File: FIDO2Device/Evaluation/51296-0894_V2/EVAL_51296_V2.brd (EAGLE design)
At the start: 25 x 38 mm, 25 parts, among them CN1 51296-0894, CN2 IF_6PIN, CN3 IF_3PIN, CN4 IF_4PIN, Q1 BSS84AKQBZ, U1 RV-3028-C7

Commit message: レイアウトを修正
・裏面べたGNDのパターンを改善
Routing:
- net VDD: track 56.7 -> 61.6 mm, vias 5 -> 6
- net LED_R: track 36.8 -> 36.5 mm, vias 1 -> 2
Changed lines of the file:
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@@
 </element>
 <element name="R1" library="Parts" package="R0402N" value="5.1k" x="6.9" y="13.8" smashed="yes" rot="R180">
-<attribute name="NAME" x="8.3" y="13.5" size="0.6" layer="25"/>
+<attribute name="NAME" x="5.4" y="14" size="0.6" layer="25" rot="R180"/>
 <attribute name="VALUE" x="7.4" y="15.1" size="0.6" layer="27" rot="R180"/>
 </element>
 <element name="R2" library="Parts" package="R0402N" value="20k" x="6.9" y="12.2" smashed="yes">
-<attribute name="NAME" x="8.3" y="11.9" size="0.6" layer="25"/>
+<attribute name="NAME" x="5.4" y="12.4" size="0.6" layer="25" rot="R180"/>
 <attribute name="VALUE" x="6.4" y="10.9" size="0.6" layer="27"/>
 </element>
@@
 <via x="11.45" y="9" extent="1-16" drill="0.3"/>
 <via x="15.3" y="5.2" extent="1-16" drill="0.3"/>
-<via x="8.8" y="10" extent="1-16" drill="0.3"/>
-<wire x1="9" y1="9.8" x2="10.65" y2="9.8" width="0.2032" layer="16"/>
-<wire x1="11.45" y1="9" x2="10.65" y2="9.8" width="0.2032" layer="16"/>
+<via x="8.6" y="12.2" extent="1-16" drill="0.3"/>
 <wire x1="11.45" y1="7.8" x2="11.45" y2="9" width="0.2032" layer="1"/>
 <wire x1="15.3" y1="5.2" x2="13" y2="5.2" width="0.2032" layer="16"/>
@@
 <wire x1="13.55" y1="11.1" x2="11.45" y2="9" width="0.2032" layer="16"/>
 <wire x1="15.95" y1="10.95" x2="16.4" y2="11.4" width="0.2032" layer="1"/>
-<wire x1="9" y1="9.8" x2="8.8" y2="10" width="0.2032" layer="16"/>
-<wire x1="8.6" y1="10.2" x2="8.8" y2="10" width="0.2032" layer="1"/>
 <contactref element="D2" pad="1"/>
 <contactref element="R6" pad="2"/>
@@
 <contactref element="R11" pad="2"/>
 <via x="5.4" y="10" extent="1-16" drill="0.3"/>
-<wire x1="6.4" y1="9.875" x2="5.825" y2="9.875" width="0.2032" layer="1"/>
-<wire x1="5.825" y1="9.875" x2="5.7" y2="10" width="0.2032" layer="1"/>
-<wire x1="5.4" y1="10" x2="8.8" y2="10" width="0.2032" layer="16"/>
-<wire x1="5.4" y1="10" x2="5.7" y2="10" width="0.2032" layer="1"/>
-<wire x1="5.825" y1="9.875" x2="5.825" y2="4.625" width="0.2032" layer="1"/>
-<wire x1="5.825" y1="4.625" x2="5.35" y2="4.15" width="0.2032" layer="1"/>
+<wire x1="5.725" y1="4.525" x2="5.35" y2="4.15" width="0.2032" layer="1"/>
 <wire x1="4.65" y1="4.15" x2="5.35" y2="4.15" width="0.2032" layer="1"/>
 <wire x1="15.95" y1="10.95" x2="15.1" y2="10.95" width="0.2032" layer="1"/>
-<wire x1="8.6" y1="10.2" x2="8.6" y2="11.9" width="0.2032" layer="1"/>
-<wire x1="8.3" y1="12.2" x2="8.6" y2="11.9" width="0.2032" layer="1"/>
 <wire x1="16" y1="2.9" x2="16" y2="4.5" width="0.2032" layer="1"/>
 <wire x1="16" y1="4.5" x2="15.3" y2="5.2" width="0.2032" layer="1"/>
@@
 <wire x1="15.95" y1="10.95" x2="16" y2="10.95" width="0.2032" layer="1"/>
 <wire x1="16" y1="10.95" x2="16.65" y2="10.3" width="0.2032" layer="1"/>
-<wire x1="7.6" y1="12.2" x2="7.1" y2="12.2" width="0.2032" layer="1"/>
 <wire x1="7.1" y1="12.2" x2="6.9" y2="12.4" width="0.2032" layer="1"/>
 <wire x1="6.9" y1="12.4" x2="6.9" y2="15.4" width="0.2032" layer="1"/>
-<wire x1="8.3" y1="12.2" x2="7.6" y2="12.2" width="0.2032" layer="1"/>
 <wire x1="2.8" y1="26.5" x2="2.8" y2="23.74" width="0.2032" layer="1"/>
 <wire x1="6.9" y1="15.4" x2="3.9" y2="18.4" width="0.2032" layer="1"/>
 <wire x1="3.9" y1="18.4" x2="3.9" y2="22.64" width="0.2032" layer="1"/>
 <wire x1="3.9" y1="22.64" x2="2.8" y2="23.74" width="0.2032" layer="1"/>
+<wire x1="6.4" y1="9.875" x2="5.525" y2="9.875" width="0.2032" layer="1"/>
+<wire x1="5.525" y1="9.875" x2="5.4" y2="10" width="0.2032" layer="1"/>
+<wire x1="5.525" y1="9.875" x2="5.525" y2="9.375" width="0.2032" layer="1"/>
+<wire x1="5.525" y1="9.375" x2="6.3" y2="8.6" width="0.2032" layer="1"/>
+<wire x1="6.3" y1="8.6" x2="7.5" y2="8.6" width="0.2032" layer="1"/>
+<wire x1="7.5" y1="8.6" x2="7.9" y2="8.2" width="0.2032" layer="1"/>
+<via x="10.7" y="6.9" extent="1-16" drill="0.3"/>
+<wire x1="10.7" y1="6.9" x2="8.2" y2="6.9" width="0.2032" layer="1"/>
+<wire x1="8.2" y1="6.9" x2="7.9" y2="7.2" width="0.2032" layer="1"/>
+<wire x1="7.9" y1="7.2" x2="7.9" y2="8.2" width="0.2032" layer="1"/>
+<wire x1="5.725" y1="4.525" x2="5.725" y2="8.025" width="0.2032" layer="1"/>
+<wire x1="5.725" y1="8.025" x2="6.3" y2="8.6" width="0.2032" layer="1"/>
+<wire x1="13" y1="5.2" x2="12.4" y2="5.2" width="0.2032" layer="16"/>
+<wire x1="12.4" y1="5.2" x2="10.7" y2="6.9" width="0.2032" layer="16"/>
+<wire x1="8.6" y1="12.2" x2="7.3" y2="12.2" width="0.2032" layer="16"/>
+<wire x1="7.3" y1="12.2" x2="5.4" y2="10.3" width="0.2032" layer="16"/>
+<wire x1="5.4" y1="10" x2="5.4" y2="10.3" width="0.2032" layer="16"/>
+<wire x1="7.6" y1="12.2" x2="8.6" y2="12.2" width="0.2032" layer="1"/>
+<wire x1="7.1" y1="12.2" x2="7.6" y2="12.2" width="0.2032" layer="1"/>
 </signal>
 <signal name="LED_CTRL">
@@
 <wire x1="20" y1="34.3" x2="21.2" y2="35.5" width="0.2032" layer="16"/>
 <via x="5.6" y="14.7" extent="1-16" drill="0.3"/>
-<wire x1="8.8" y1="17.8" x2="8.8" y2="18.3" width="0.2032" layer="16"/>
-<wire x1="8.8" y1="18.3" x2="8.8" y2="19.2" width="0.2032" layer="16"/>
-<wire x1="8.8" y1="19.2" x2="9.8" y2="20.2" width="0.2032" layer="16"/>
-<wire x1="9.8" y1="20.2" x2="9.8" y2="23.74" width="0.2032" layer="16"/>
 <wire x1="4.2" y1="9.5" x2="4.2" y2="11.4" width="0.2032" layer="1"/>
 <wire x1="4.2" y1="11.4" x2="5.4" y2="12.6" width="0.2032" layer="1"/>
 <wire x1="5.4" y1="12.6" x2="5.4" y2="14.5" width="0.2032" layer="1"/>
 <wire x1="5.4" y1="14.5" x2="5.6" y2="14.7" width="0.2032" layer="1"/>
-<wire x1="5.6" y1="14.7" x2="6.2" y2="14.7" width="0.2032" layer="16"/>
-<wire x1="6.2" y1="14.7" x2="8.8" y2="17.3" width="0.2032" layer="16"/>
-<wire x1="8.8" y1="17.3" x2="8.8" y2="17.8" width="0.2032" layer="16"/>
+<via x="7.5" y="16.6" extent="1-16" drill="0.3"/>
+<wire x1="7.5" y1="16.6" x2="8.7" y2="17.8" width="0.2032" layer="1"/>
+<wire x1="8.7" y1="17.8" x2="8.7" y2="19.1" width="0.2032" layer="1"/>
+<wire x1="8.7" y1="19.1" x2="9.8" y2="20.2" width="0.2032" layer="1"/>
+<wire x1="9.8" y1="20.2" x2="9.8" y2="23.74" width="0.2032" layer="1"/>
+<wire x1="5.6" y1="14.7" x2="7.5" y2="16.6" width="0.2032" layer="16"/>
 </signal>
 <signal name="LED_G">

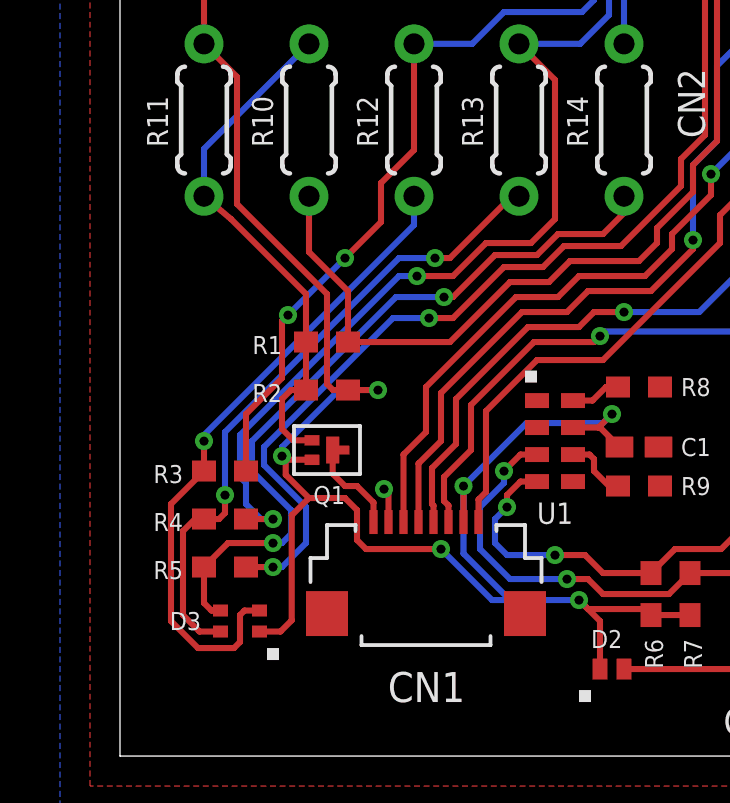
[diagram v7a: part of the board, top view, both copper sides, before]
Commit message: レイアウトを修正
・テストによって差し替える可能性がある部品と、viaを離して配置させるよう修正
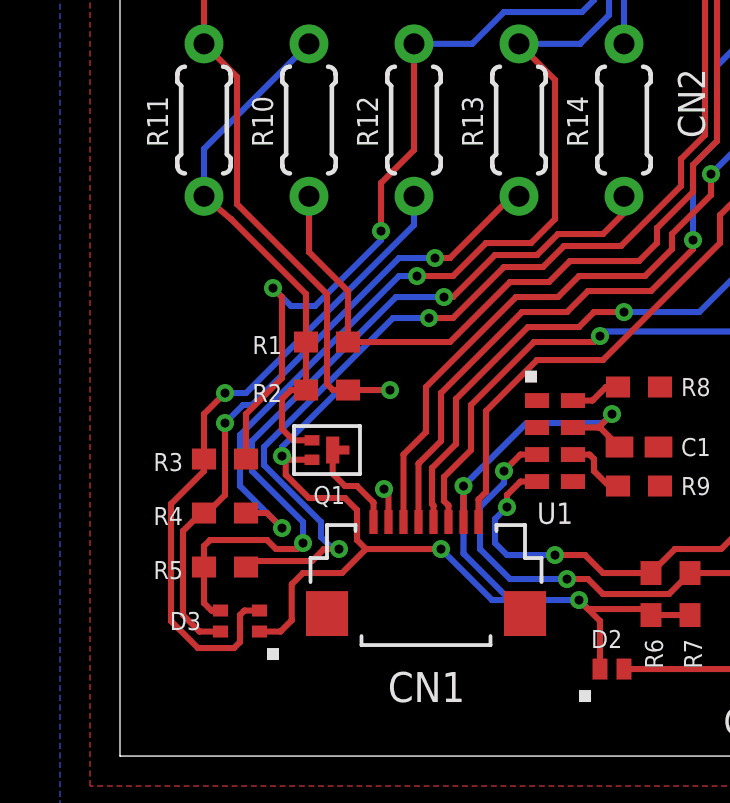
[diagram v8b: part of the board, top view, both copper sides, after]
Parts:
- moved R3 0.40 mm to (3.50, 9.90)
- moved R4 0.20 mm to (3.50, 8.10)
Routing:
- net LED_B: track 46.1 -> 47.9 mm
- net LED_R: track 36.5 -> 38.0 mm
- net N$10: track 25.0 -> 26.4 mm
- net LED_G: track 38.7 -> 39.4 mm
- net VDD: track 61.6 -> 62.2 mm
